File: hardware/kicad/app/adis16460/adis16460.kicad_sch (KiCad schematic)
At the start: 2 parts, among them J1 TOP, J2 BUTTOM

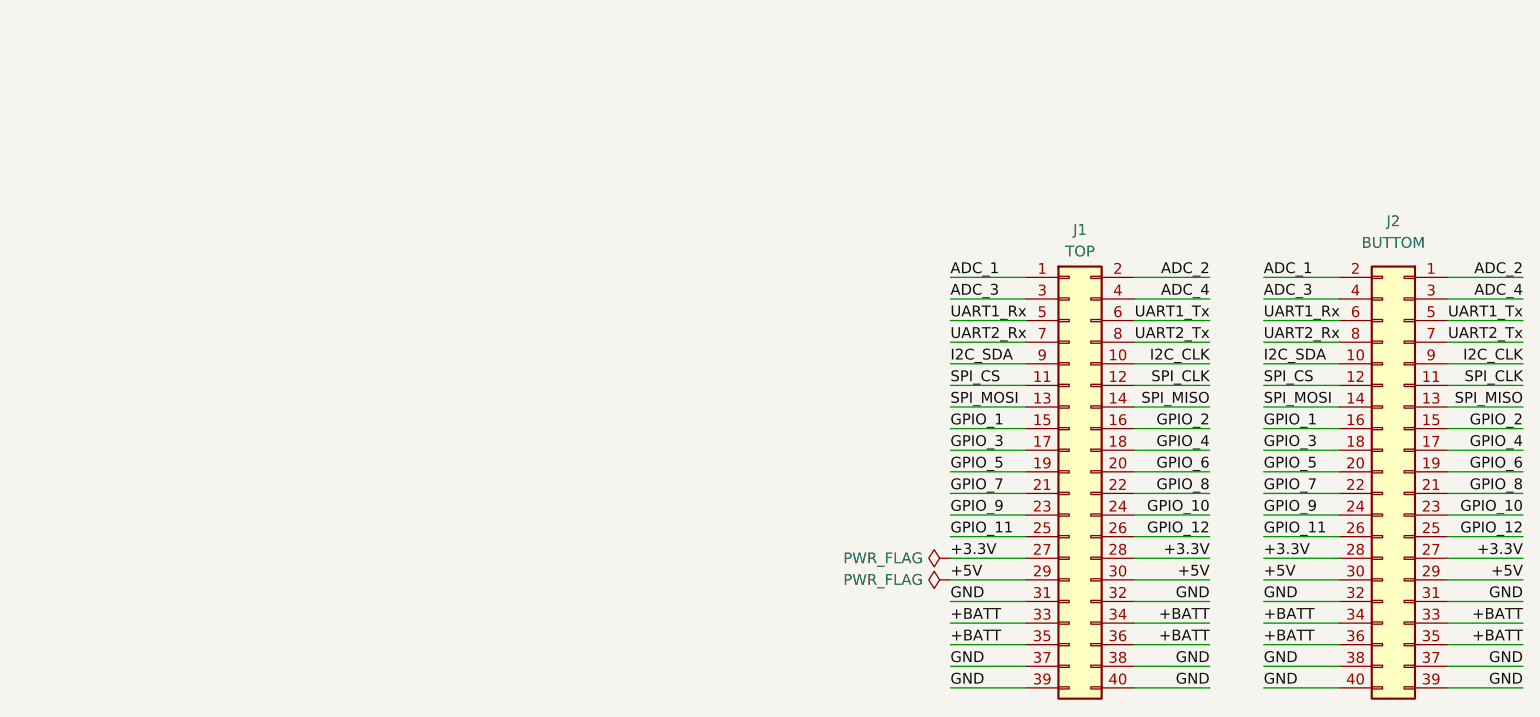
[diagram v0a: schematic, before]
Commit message: 新增APP板 ADIS16460
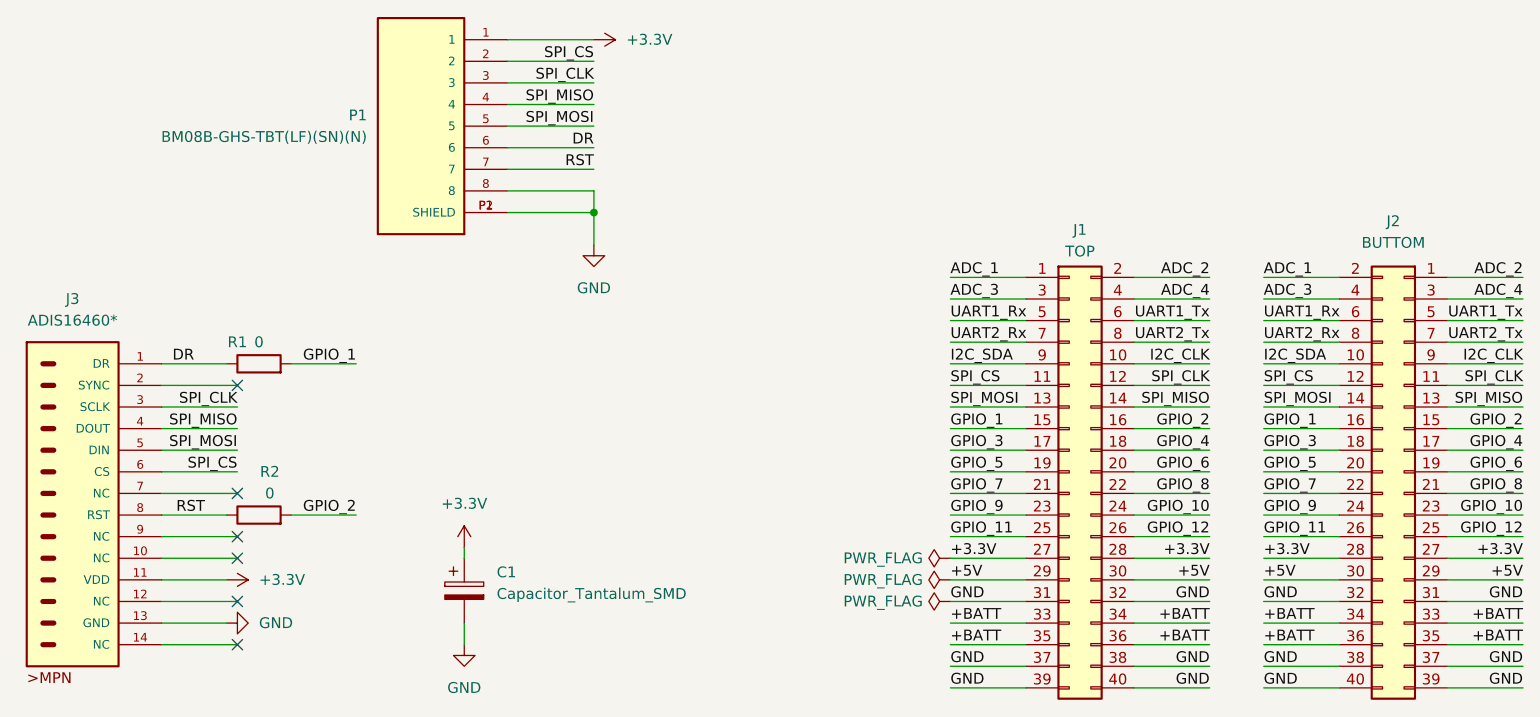
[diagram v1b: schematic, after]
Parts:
- added C1: Capacitor_Tantalum_SMD, Capacitor_Tantalum_SMD:CP_EIA-3216-12_Kemet-S, symbol Device:C_Polarized
- added J3: ADIS16460*, ADIS16460, symbol ADIS16460_:ADIS16460*
- added P1: BM08B-GHS-TBT(LF)(SN)(N), JST-GH-1.25:JST-GHS-1.25-BM08B, symbol JST-GHS-1.25-BM08B:BM08B-GHS-TBT(LF)(SN)(N)
- added R1, R2: 0, Resistor_SMD:R_0805_2012Metric, symbol Device:R
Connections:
- net +3.3V: now also C1.1, J3.11 (VDD), P1.1
- net GND: now also C1.2, J3.13 (GND), P1.8, P1.P1 (SHIELD), P1.P2 (SHIELD)
- net GPIO_1: now also R1.2
- net GPIO_2: now also R2.2
- net SPI_CLK: now also J3.3 (SCLK), P1.3
- net SPI_CS: now also J3.6 (CS), P1.2
- net SPI_MISO: now also J3.4 (DOUT), P1.4
- net SPI_MOSI: now also J3.5 (DIN), P1.5
- new net DR: J3.1 (DR), P1.6, R1.1
- new net RST: J3.8 (RST), P1.7, R2.1
- no-connect marks 0 -> 6
